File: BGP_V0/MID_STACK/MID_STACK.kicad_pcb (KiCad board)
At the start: 2 copper layers, 30 x 30 mm, 11 parts, among them P1 Conn_01x05, P2 CONN_01X12, U1 OPA170

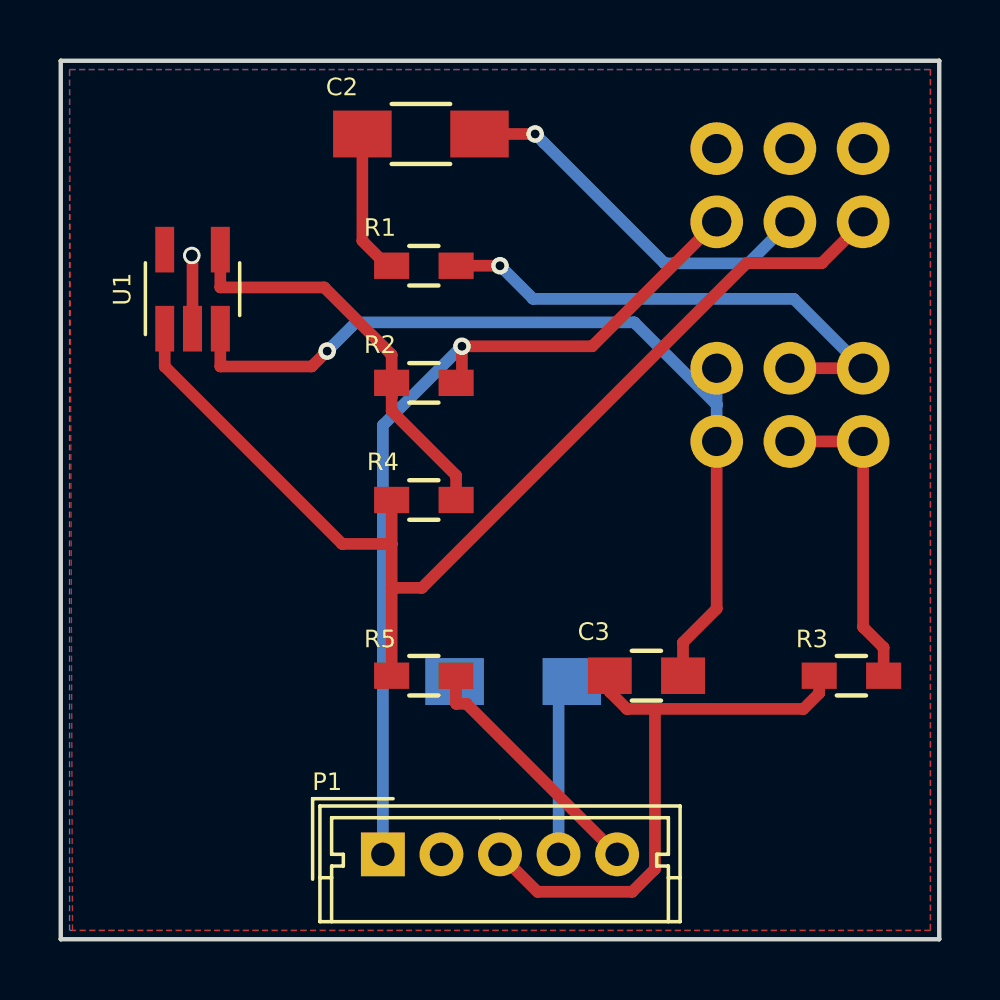
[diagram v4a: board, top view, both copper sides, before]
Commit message: Slight changes to Port layer placement - gerbers done
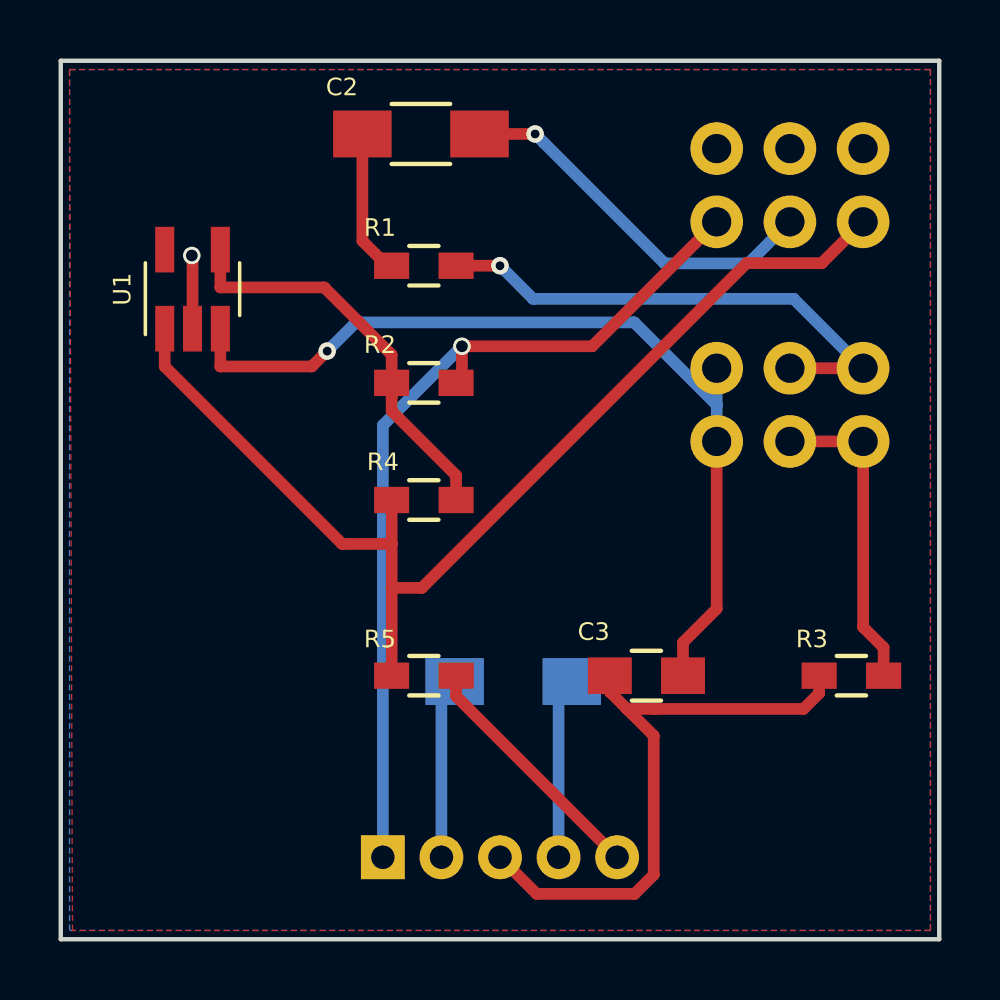
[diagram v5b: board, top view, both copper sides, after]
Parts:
- P1: moved to B.Cu
- moved P1 0.10 mm to (155.0, 91.2)
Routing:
- net /V-: track 2.51 -> 8.70 mm
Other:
- board text added: "+"
- board text added: "-"
- board text added: "G"
- board text added: "I"
- board text added: "O"
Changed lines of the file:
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@@
     (area 143.924999 63.424999 174.225001 94.979999)
     (thickness 1.6)
-    (drawings 9)
-    (tracks 74)
+    (drawings 14)
+    (tracks 76)
     (zones 0)
     (modules 11)
@@
     )
   )
-  (module Connectors_Molex:Molex_MicroLatch-53253-0570_05x2.00mm_Straight (layer F.Cu)
-    (at 155 91.1)
+  (module Connectors_Molex:Molex_MicroLatch-53253-0570_05x2.00mm_Straight (layer B.Cu)
+    (at 155 91.2)
     (descr "Molex Micro-Latch connector, PN:53253-0570, top entry type, through hole")
     (tags "conn molex micro latch")
-    (fp_text reference P1 (at -1.9 -2.475001) (layer F.SilkS)
-      (effects (font (size 0.6 0.6) (thickness 0.15)))
-    )
-    (fp_text value Conn_01x05 (at 3.9 3.024999) (layer F.Fab) hide
-      (effects (font (size 0.6 0.6) (thickness 0.15)))
-    )
-    (fp_line (start -2 -1.5) (end -2 2.15) (layer F.Fab) (width 0.1))
-    (fp_line (start -2 2.15) (end 10 2.15) (layer F.Fab) (width 0.1))
-    (fp_line (start 10 2.15) (end 10 -1.5) (layer F.Fab) (width 0.1))
-    (fp_line (start 10 -1.5) (end -2 -1.5) (layer F.Fab) (width 0.1))
-    (fp_line (start -2.6 -2.1) (end -2.6 2.75) (layer F.CrtYd) (width 0.05))
-    (fp_line (start -2.6 2.75) (end 10.65 2.75) (layer F.CrtYd) (width 0.05))
-    (fp_line (start 10.65 2.75) (end 10.65 -2.1) (layer F.CrtYd) (width 0.05))
-    (fp_line (start 10.65 -2.1) (end -2.6 -2.1) (layer F.CrtYd) (width 0.05))
-    (fp_line (start -2.15 -1.65) (end -2.15 2.3) (layer F.SilkS) (width 0.12))
-    (fp_line (start -2.15 2.3) (end 10.15 2.3) (layer F.SilkS) (width 0.12))
-    (fp_line (start 10.15 2.3) (end 10.15 -1.65) (layer F.SilkS) (width 0.12))
-    (fp_line (start 10.15 -1.65) (end -2.15 -1.65) (layer F.SilkS) (width 0.12))
-    (fp_line (start 0.35 -1.9) (end -2.4 -1.9) (layer F.SilkS) (width 0.12))
-    (fp_line (start -2.4 -1.9) (end -2.4 0.85) (layer F.SilkS) (width 0.12))
-    (fp_line (start 0.35 -1.9) (end -2.4 -1.9) (layer F.Fab) (width 0.1))
-    (fp_line (start -2.4 -1.9) (end -2.4 0.85) (layer F.Fab) (width 0.1))
-    (fp_line (start -2.15 0.8) (end -1.75 0.8) (layer F.SilkS) (width 0.12))
-    (fp_line (start 10.15 0.8) (end 9.75 0.8) (layer F.SilkS) (width 0.12))
-    (fp_line (start 4 -1.25) (end -1.75 -1.25) (layer F.SilkS) (width 0.12))
-    (fp_line (start -1.75 -1.25) (end -1.75 0) (layer F.SilkS) (width 0.12))
-    (fp_line (start -1.75 0) (end -1.35 0) (layer F.SilkS) (width 0.12))
-    (fp_line (start -1.35 0) (end -1.35 0.4) (layer F.SilkS) (width 0.12))
-    (fp_line (start -1.35 0.4) (end -1.75 0.4) (layer F.SilkS) (width 0.12))
-    (fp_line (start -1.75 0.4) (end -1.75 2.3) (layer F.SilkS) (width 0.12))
-    (fp_line (start 4 -1.25) (end 9.75 -1.25) (layer F.SilkS) (width 0.12))
-    (fp_line (start 9.75 -1.25) (end 9.75 0) (layer F.SilkS) (width 0.12))
-    (fp_line (start 9.75 0) (end 9.35 0) (layer F.SilkS) (width 0.12))
-    (fp_line (start 9.35 0) (end 9.35 0.4) (layer F.SilkS) (width 0.12))
-    (fp_line (start 9.35 0.4) (end 9.75 0.4) (layer F.SilkS) (width 0.12))
-    (fp_line (start 9.75 0.4) (end 9.75 2.3) (layer F.SilkS) (width 0.12))
-    (fp_text user %R (at 4 1.5) (layer F.Fab) hide
-      (effects (font (size 0.6 0.6) (thickness 0.15)))
+    (fp_text reference P1 (at 10.8 -2) (layer B.SilkS)
+      (effects (font (size 0.6 0.6) (thickness 0.15)) (justify mirror))
+    )
+    (fp_text value Conn_01x05 (at 3.9 -3.024999) (layer B.Fab) hide
+      (effects (font (size 0.6 0.6) (thickness 0.15)) (justify mirror))
+    )
+    (fp_line (start -2 1.5) (end -2 -2.15) (layer B.Fab) (width 0.1))
+    (fp_line (start -2 -2.15) (end 10 -2.15) (layer B.Fab) (width 0.1))
+    (fp_line (start 10 -2.15) (end 10 1.5) (layer B.Fab) (width 0.1))
+    (fp_line (start 10 1.5) (end -2 1.5) (layer B.Fab) (width 0.1))
+    (fp_line (start -2.6 2.1) (end -2.6 -2.75) (layer B.CrtYd) (width 0.05))
+    (fp_line (start -2.6 -2.75) (end 10.65 -2.75) (layer B.CrtYd) (width 0.05))
+    (fp_line (start 10.65 -2.75) (end 10.65 2.1) (layer B.CrtYd) (width 0.05))
+    (fp_line (start 10.65 2.1) (end -2.6 2.1) (layer B.CrtYd) (width 0.05))
+    (fp_line (start -2.15 1.65) (end -2.15 -2.3) (layer B.SilkS) (width 0.12))
+    (fp_line (start -2.15 -2.3) (end 10.15 -2.3) (layer B.SilkS) (width 0.12))
+    (fp_line (start 10.15 -2.3) (end 10.15 1.65) (layer B.SilkS) (width 0.12))
+    (fp_line (start 10.15 1.65) (end -2.15 1.65) (layer B.SilkS) (width 0.12))
+    (fp_line (start 0.35 1.9) (end -2.4 1.9) (layer B.SilkS) (width 0.12))
+    (fp_line (start -2.4 1.9) (end -2.4 -0.85) (layer B.SilkS) (width 0.12))
+    (fp_line (start 0.35 1.9) (end -2.4 1.9) (layer B.Fab) (width 0.1))
+    (fp_line (start -2.4 1.9) (end -2.4 -0.85) (layer B.Fab) (width 0.1))
+    (fp_line (start -2.15 -0.8) (end -1.75 -0.8) (layer B.SilkS) (width 0.12))
+    (fp_line (start 10.15 -0.8) (end 9.75 -0.8) (layer B.SilkS) (width 0.12))
+    (fp_line (start 4 1.25) (end -1.75 1.25) (layer B.SilkS) (width 0.12))
+    (fp_line (start -1.75 1.25) (end -1.75 0) (layer B.SilkS) (width 0.12))
+    (fp_line (start -1.75 0) (end -1.35 0) (layer B.SilkS) (width 0.12))
+    (fp_line (start -1.35 0) (end -1.35 -0.4) (layer B.SilkS) (width 0.12))
+    (fp_line (start -1.35 -0.4) (end -1.75 -0.4) (layer B.SilkS) (width 0.12))
+    (fp_line (start -1.75 -0.4) (end -1.75 -2.3) (layer B.SilkS) (width 0.12))
+    (fp_line (start 4 1.25) (end 9.75 1.25) (layer B.SilkS) (width 0.12))
+    (fp_line (start 9.75 1.25) (end 9.75 0) (layer B.SilkS) (width 0.12))
+    (fp_line (start 9.75 0) (end 9.35 0) (layer B.SilkS) (width 0.12))
+    (fp_line (start 9.35 0) (end 9.35 -0.4) (layer B.SilkS) (width 0.12))
+    (fp_line (start 9.35 -0.4) (end 9.75 -0.4) (layer B.SilkS) (width 0.12))
+    (fp_line (start 9.75 -0.4) (end 9.75 -2.3) (layer B.SilkS) (width 0.12))
+    (fp_text user %R (at 4 -1.5) (layer B.Fab) hide
+      (effects (font (size 0.6 0.6) (thickness 0.15)) (justify mirror))
     )
     (pad 1 thru_hole rect (at 0 0) (size 1.5 1.5) (drill 0.8) (layers *.Cu *.Mask)
@@
     )
   )
+  (gr_text O (at 163 88) (layer B.SilkS)
+    (effects (font (size 0.6 0.6) (thickness 0.15)) (justify mirror))
+  )
+  (gr_text + (at 161 88) (layer B.SilkS)
+    (effects (font (size 0.6 0.6) (thickness 0.15)) (justify mirror))
+  )
+  (gr_text G (at 159 88) (layer B.SilkS)
+    (effects (font (size 0.6 0.6) (thickness 0.15)) (justify mirror))
+  )
+  (gr_text - (at 157 88) (layer B.SilkS)
+    (effects (font (size 0.6 0.6) (thickness 0.15)) (justify mirror))
+  )
+  (gr_text I (at 155 88) (layer B.SilkS)
+    (effects (font (size 0.6 0.6) (thickness 0.15)) (justify mirror))
+  )
   (gr_text "BGP V0.0\nMid Stack\n" (at 148 66) (layer B.SilkS)
     (effects (font (size 0.6 0.6) (thickness 0.15)) (justify mirror))
@@
   (gr_line (start 144 64) (end 144 94) (angle 90) (layer Edge.Cuts) (width 0.15))
   (gr_line (start 174 64) (end 144 64) (angle 90) (layer Edge.Cuts) (width 0.15))
+  (segment (start 161 91.2) (end 161 85.65) (width 0.4) (layer B.Cu) (net 1))
   (segment (start 161 85.65) (end 161.45 85.2) (width 0.4) (layer B.Cu) (net 1))
-  (segment (start 161 91.1) (end 161 85.65) (width 0.4) (layer B.Cu) (net 1))
-  (segment (start 160.28 92.3798) (end 159 91.1) (width 0.4) (layer F.Cu) (net 2))
-  (segment (start 163.515 92.3798) (end 160.28 92.3798) (width 0.4) (layer F.Cu) (net 2))
-  (segment (start 164.292 91.6023) (end 163.515 92.3798) (width 0.4) (layer F.Cu) (net 2))
-  (segment (start 164.292 86.1353) (end 164.292 91.6023) (width 0.4) (layer F.Cu) (net 2))
+  (segment (start 159 91.2) (end 160.250001 92.450001) (width 0.4) (layer F.Cu) (net 2))
+  (segment (start 160.250001 92.450001) (end 163.600001 92.450001) (width 0.4) (layer F.Cu) (net 2))
+  (segment (start 163.600001 92.450001) (end 164.250001 91.800001) (width 0.4) (layer F.Cu) (net 2))
+  (segment (start 164.250001 91.800001) (end 164.250001 87.050301) (width 0.4) (layer F.Cu) (net 2))
+  (segment (start 164.250001 87.050301) (end 163.335 86.1353) (width 0.4) (layer F.Cu) (net 2))
   (segment (start 169.365 86.1353) (end 164.292 86.1353) (width 0.4) (layer F.Cu) (net 2))
   (segment (start 169.9 85.6) (end 169.365 86.1353) (width 0.4) (layer F.Cu) (net 2))
@@
   (segment (start 154.3 70.15) (end 155.15 71) (width 0.4) (layer F.Cu) (net 3))
   (segment (start 154.3 66.5) (end 154.3 70.15) (width 0.4) (layer F.Cu) (net 3))
-  (via (at 157.7 73.75) (size 0.6) (layers F.Cu B.Cu) (net 4))
+  (segment (start 155 91.2) (end 155 76.45) (width 0.4) (layer B.Cu) (net 4))
+  (via (at 157.7 73.75) (size 0.6) (drill 0.4) (layers F.Cu B.Cu) (net 4))
+  (segment (start 155 76.45) (end 157.7 73.75) (width 0.4) (layer B.Cu) (net 4))
   (segment (start 157.7 74.8) (end 157.5 75) (width 0.4) (layer F.Cu) (net 4))
   (segment (start 157.7 73.75) (end 157.7 74.8) (width 0.4) (layer F.Cu) (net 4))
-  (segment (start 155 76.45) (end 155 91.1) (width 0.4) (layer B.Cu) (net 4))
-  (segment (start 157.7 73.75) (end 155 76.45) (width 0.4) (layer B.Cu) (net 4))
   (segment (start 162.15 73.75) (end 166.4 69.5) (width 0.4) (layer F.Cu) (net 4))
   (segment (start 157.7 73.75) (end 162.15 73.75) (width 0.4) (layer F.Cu) (net 4))
-  (segment (start 157.86 85.9603) (end 163 91.1) (width 0.4) (layer F.Cu) (net 5))
-  (segment (start 157.5 85.9603) (end 157.86 85.9603) (width 0.4) (layer F.Cu) (net 5))
-  (segment (start 157.5 85) (end 157.5 85.9603) (width 0.4) (layer F.Cu) (net 5))
+  (segment (start 163 91.2) (end 157.5 85.7) (width 0.4) (layer F.Cu) (net 5))
+  (segment (start 157.5 85.7) (end 157.5 85) (width 0.4) (layer F.Cu) (net 5))
+  (segment (start 157 91.2) (end 157 85.65) (width 0.4) (layer B.Cu) (net 6))
+  (segment (start 157 85.65) (end 157.45 85.2) (width 0.4) (layer B.Cu) (net 6))
   (segment (start 148.5 70.674974) (end 148.475026 70.65) (width 0.4) (layer F.Cu) (net 6))
   (segment (start 148.5 73.15) (end 148.5 70.674974) (width 0.4) (layer F.Cu) (net 6))
